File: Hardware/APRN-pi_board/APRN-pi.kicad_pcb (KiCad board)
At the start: 2 copper layers, 65 x 56.5 mm, 31 parts, among them J1 Raspberry_Pi_2_3, J2 Conn_Coaxial, J3 Amplifier Jumper, J4 Screw_Terminal_01x02, J5 AudioJack4, Q1 MMBT3906, U1 DRA818V, U2 L7805

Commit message: Add thanks
@ka2qfx
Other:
- board text added: "Made with help from KA2QFX and others And: #hamradio on libera.chat https://github.com/KenwoodFox/APRN-pi"
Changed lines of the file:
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@@
   (gr_line (start 109 118.5) (end 109 68) (layer "Edge.Cuts") (width 0.1))
   (gr_line (start 171 121.5) (end 112 121.5) (layer "Edge.Cuts") (width 0.1))
+  (gr_text "Made with help from KA2QFX and others\n\nAnd:\n#hamradio on libera.chat\n\nhttps://github.com/KenwoodFox/APRN-pi" (at 139.5 79.5) (layer "B.SilkS")
+    (effects (font (size 1.5 1.5) (thickness 0.3)) (justify mirror))
+  )
   (gr_text "APRN-Pi\nDesign by KW1FOX\n${FULL_REVISION}" (at 154.5 85) (layer "F.SilkS")
     (effects (font (size 1.27 1.27) (thickness 0.15)) (justify left))

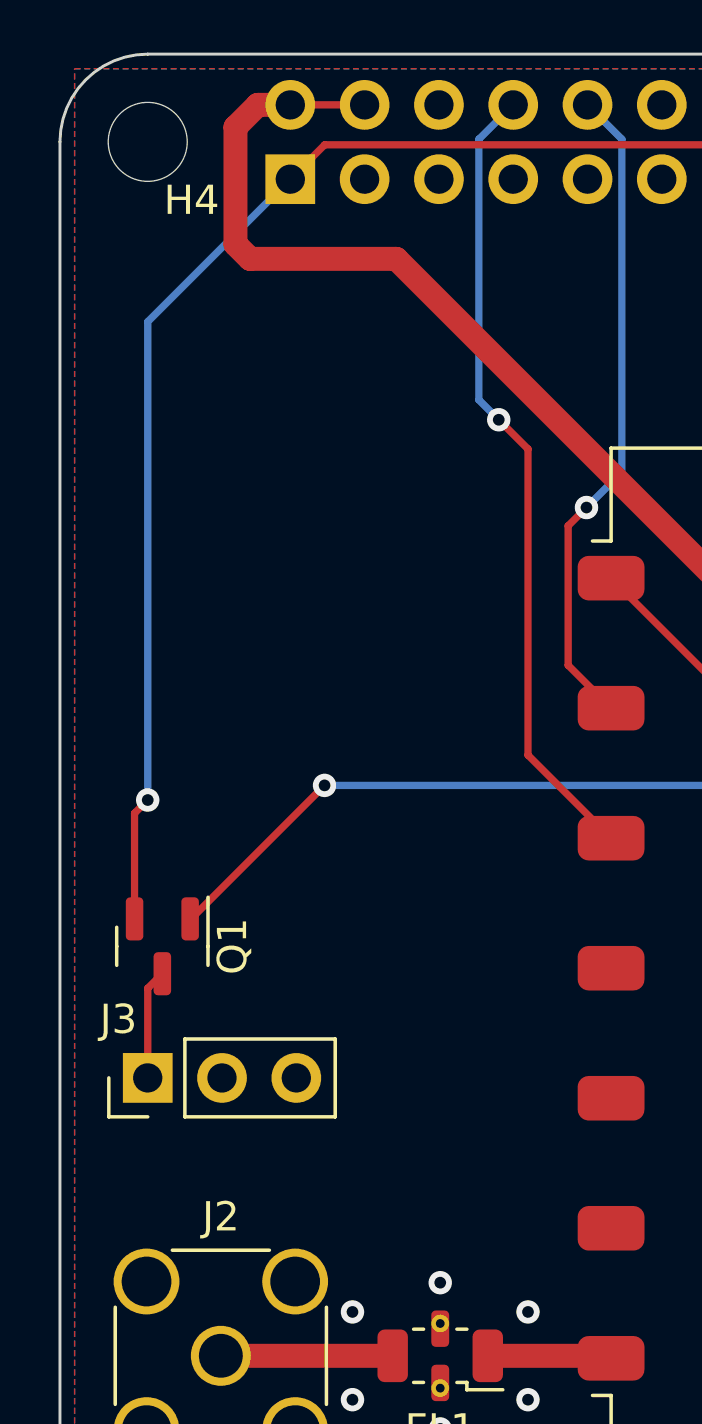
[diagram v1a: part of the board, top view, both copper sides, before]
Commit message: add i2c breakout
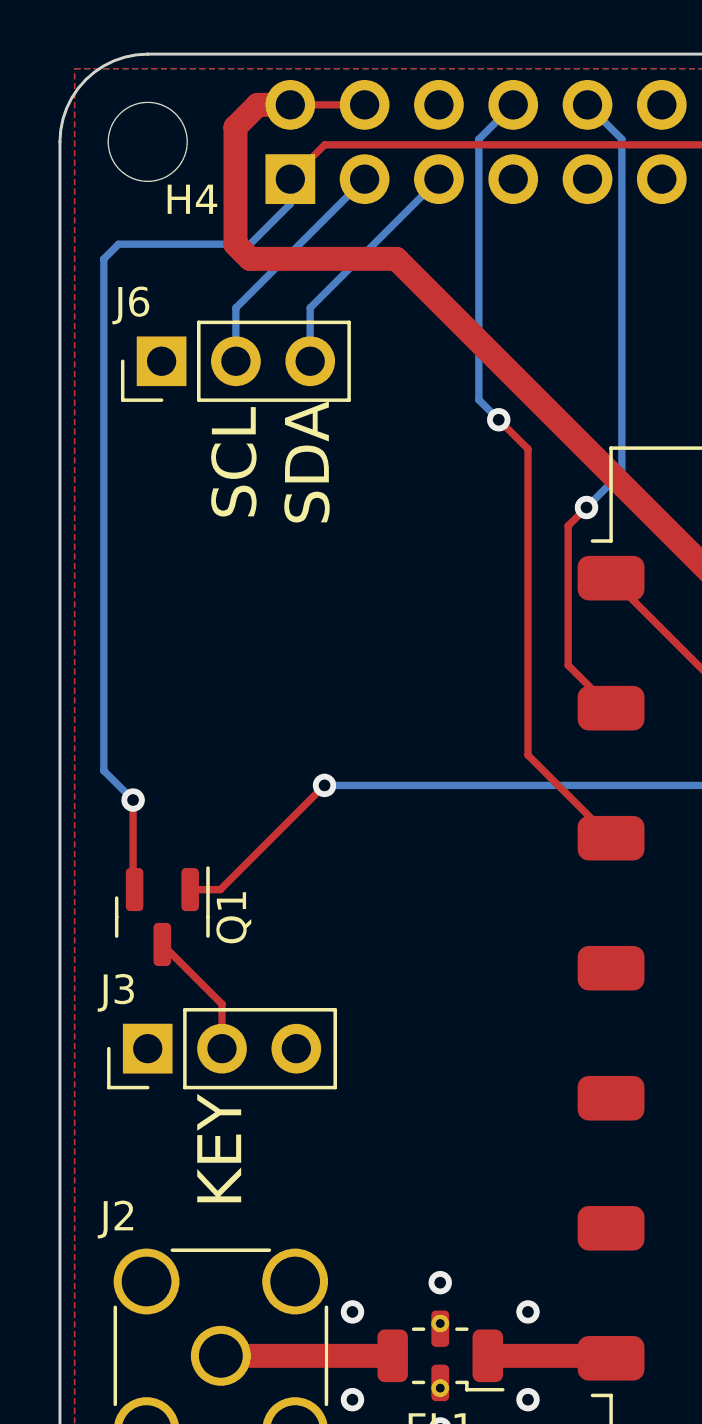
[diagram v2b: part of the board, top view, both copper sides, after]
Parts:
- added J6: i2c Jumper, Connector_PinHeader_2.54mm:PinHeader_1x03_P2.54mm_Vertical, F.Cu at (112.5, 75.5)
- moved J3 1.00 mm to (112.0, 99.0)
- moved Q1 1.00 mm to (112.5, 94.5)
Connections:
- J1 pad 3: unconnected-(J1-Pad3) -> SCL
- J1 pad 5: unconnected-(J1-Pad5) -> SDA
- J3 pad 1: Net-(J3-Pad1) -> GND
- J3 pad 2: GND -> Net-(J3-Pad2)
- J3 pad 3: unconnected-(J3-Pad3) -> GND
- Q1 pad 3: Net-(J3-Pad1) -> Net-(J3-Pad2)
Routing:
- net SCL: track 0.00 -> 8.05 mm
- net SDA: track 0.00 -> 8.05 mm
- net Net-(J3-Pad2): track 0.00 -> 4.41 mm
- net Net-(J3-Pad1): track 3.77 -> 0.00 mm
- net +3V3: track 84.3 -> 86.9 mm
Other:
- board text added: "KEY"
- board text added: "SCL"
- board text added: "SDA"

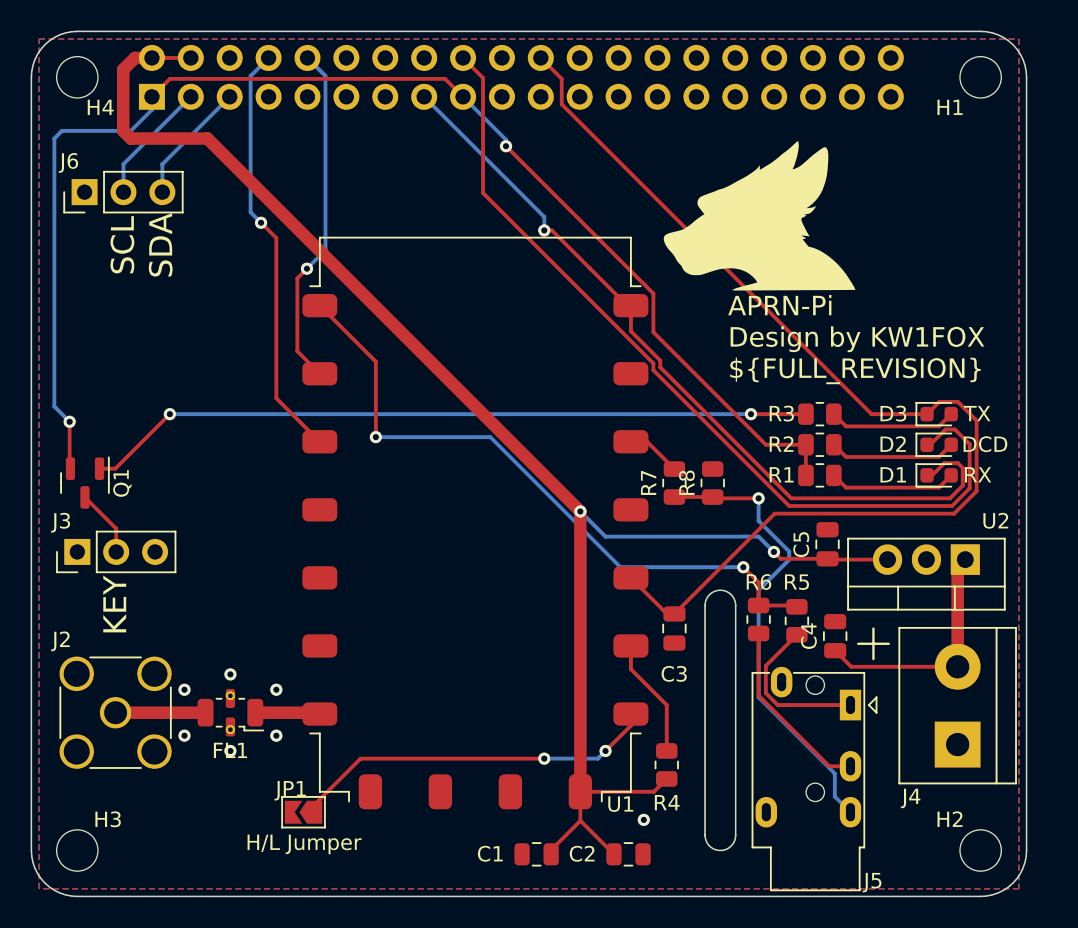
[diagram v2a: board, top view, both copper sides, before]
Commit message: This board will tottally need a rewiring
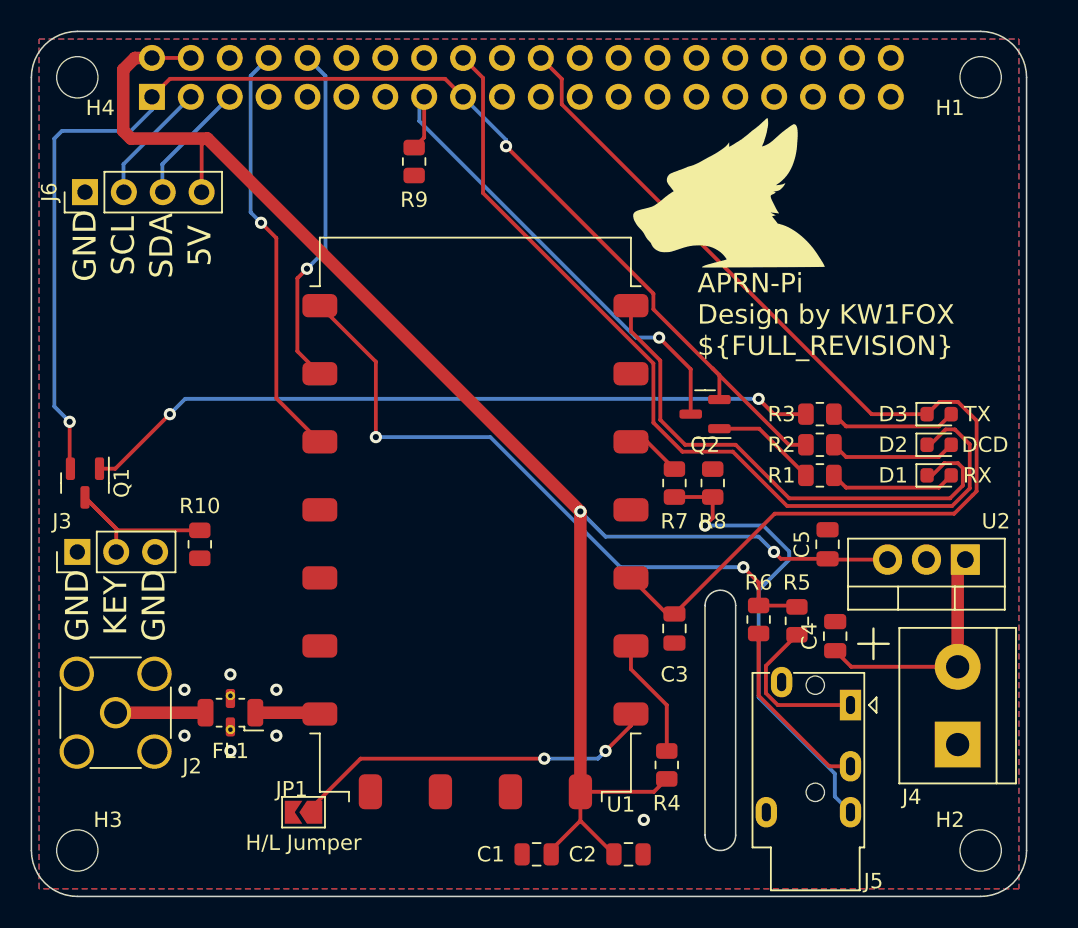
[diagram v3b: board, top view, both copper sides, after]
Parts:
- added Q2: MMBT3906, Package_TO_SOT_SMD:SOT-23, F.Cu at (153.0, 90.0)
- added R10: 10k, Resistor_SMD:R_0805_2012Metric, F.Cu at (120.0, 98.5)
- added R9: 10k, Resistor_SMD:R_0805_2012Metric, F.Cu at (134.0, 73.5)
- J6: value i2c Jumper -> Conn_01x04; footprint Connector_PinHeader_2.54mm:PinHeader_1x03_P2.54mm_Vertical -> Connector_PinHeader_2.54mm:PinHeader_1x04_P2.54mm_Vertical
- moved L1 2.50 mm to (154.5, 75.5)
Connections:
- D1 pad 1: GPIO22 -> SQL
- J6 pad 2: SCL -> SDA
- J6 pad 3: SDA -> SCL
- R1 pad 1: +3V3 -> Net-(R1-Pad1)
- U1 pad 1: GPIO22 -> SQL
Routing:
- net SQL: track 0.00 -> 34.7 mm
- net GPIO22: track 52.1 -> 32.2 mm
- net Net-(Q1-Pad3): track 4.41 -> 12.8 mm
- net Net-(R1-Pad1): track 0.00 -> 6.91 mm
- net +5V: track 102.5 -> 106.2 mm
- net GPIO24: track 56.8 -> 58.8 mm
- net Net-(J5-PadR2): track 30.2 -> 31.1 mm
- net Net-(Q1-Pad1): track 47.6 -> 48.4 mm
- net +3V3: track 86.9 -> 86.2 mm
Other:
- board text added: "5V"
- board text added: "GND"

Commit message: misc
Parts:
- moved L1 1.00 mm to (155.5, 75.5)
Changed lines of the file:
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@@
   )
   (footprint "KenwoodFox:KITSUNE_LOGO" (layer "F.Cu")
-    (at 154.5 75.5)
+    (at 155.5 75.5)
     (property "Sheetfile" "APRN-pi.kicad_sch")
     (property "Sheetname" "")
@@
     (effects (font (size 1.5 1.5) (thickness 0.3)))
   )
-  (gr_text "APRN-Pi\nDesign by KW1FOX\n${FULL_REVISION}" (at 152.5 83.5) (layer "F.SilkS")
+  (gr_text "APRN-Pi\nDesign by KW1FOX\n${FULL_REVISION}" (at 153.5 83.5) (layer "F.SilkS")
     (effects (font (size 1.27 1.27) (thickness 0.15)) (justify left))
   )

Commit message: more logos
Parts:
- added L2: KITSUNE_LOGO, KenwoodFox:KITSUNE_LOGO, B.Cu at (134.5, 92.5)
- added REF**: OSHW-Symbol_8.9x8mm_SilkScreen, Symbol:OSHW-Symbol_8.9x8mm_SilkScreen, B.Cu at (146.5, 92.5)

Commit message: Use upstream
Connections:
- J6 pad 2: SDA -> SCL
- J6 pad 3: SCL -> SDA
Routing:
- net Net-(R4-Pad1): track 7.83 -> 8.49 mm

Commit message: Do some pcb layout
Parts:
- moved C5 2.69 mm to (158.5, 97.5), turned to 180 degrees
- moved R7 1.41 mm to (150.0, 95.5)
- moved R8 1.41 mm to (152.5, 95.5)
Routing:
- net GPIO25: track 71.4 -> 66.6 mm, vias 0 -> 2
- net +5V: track 106.2 -> 109.2 mm, vias 2 -> 0
- net Net-(J5-PadR2): track 31.1 -> 29.9 mm
- net TX_AUDIO: track 42.8 -> 41.9 mm
- net Net-(C4-Pad1): track 15.6 -> 16.3 mm
- net GND: vias 7 -> 9

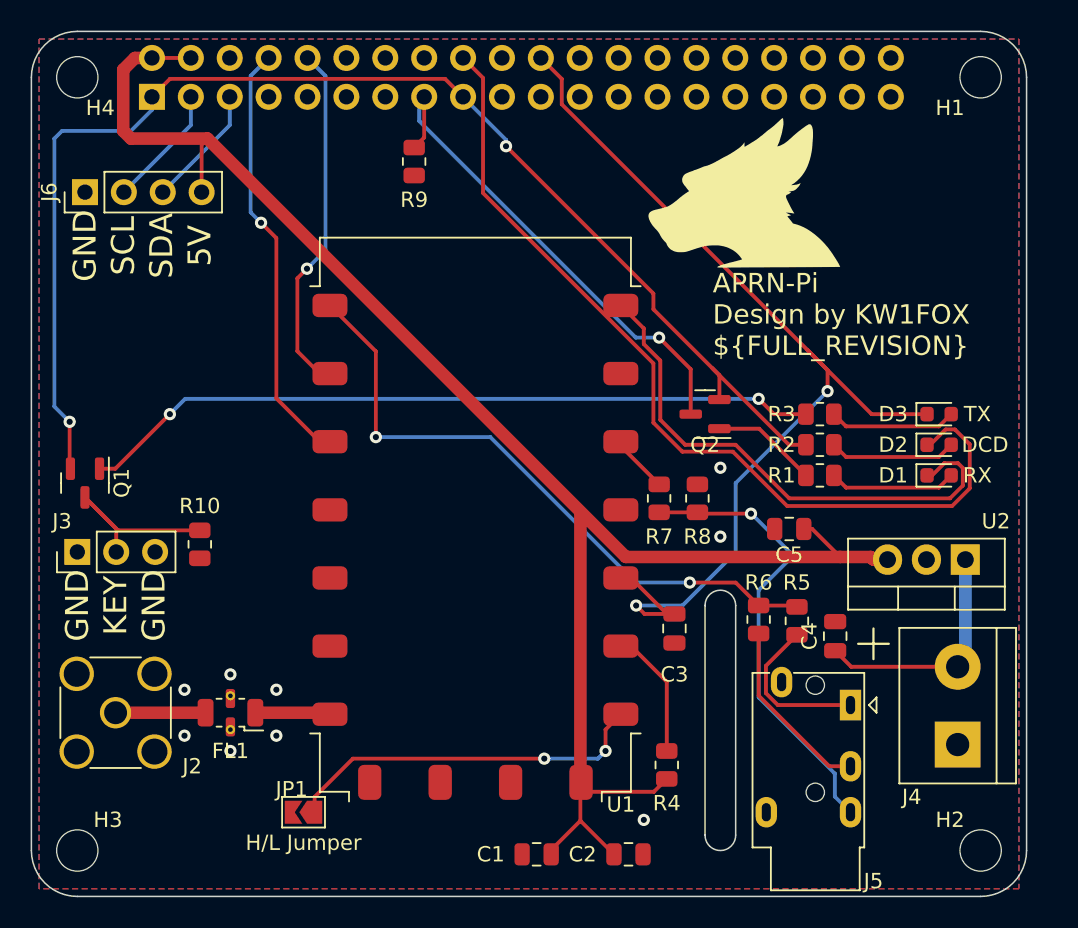
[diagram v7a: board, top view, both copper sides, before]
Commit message: Refactor wiring
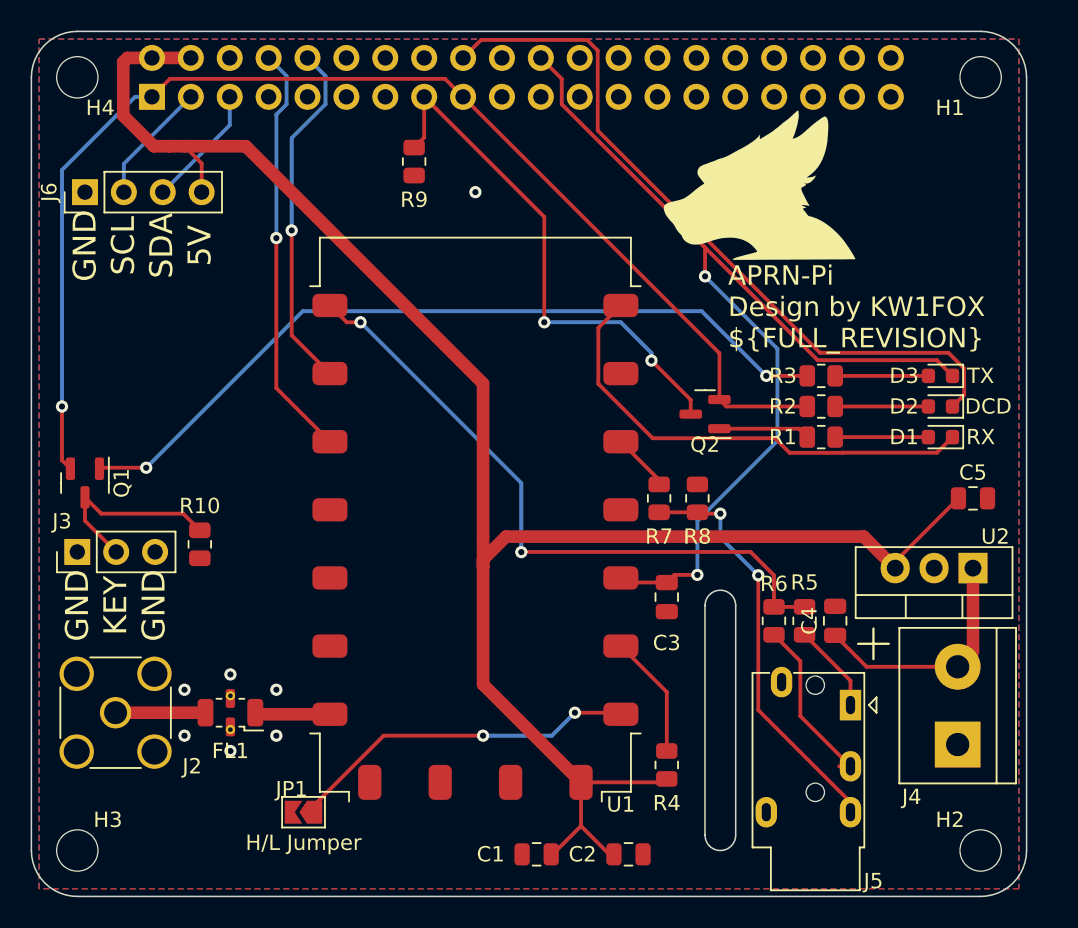
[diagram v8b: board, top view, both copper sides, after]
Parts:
- moved C5 12.2 mm to (170.5, 95.5), turned to 0 degrees
- moved D1 2.50 mm to (168.4, 91.5), turned to 180 degrees
- moved D2 2.50 mm to (168.4, 89.5), turned to 180 degrees
- moved D3 2.50 mm to (168.4, 87.5), turned to 180 degrees
- moved R1 2.50 mm to (160.6, 91.5)
- moved R2 2.50 mm to (160.6, 89.5)
- moved R3 2.50 mm to (160.6, 87.5)
- moved C3 2.11 mm to (150.5, 102.0)
- moved L1 1.12 mm to (156.5, 75.0)
- moved R6 1.00 mm to (157.5, 103.5)
- moved C4 1.00 mm to (161.5, 103.5)
- moved U2 0.75 mm to (170.5, 100.1)
- moved R5 0.50 mm to (159.5, 103.5)
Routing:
- net +5V: track 109.2 -> 120.6 mm
- net GPIO24: track 58.8 -> 48.0 mm
- net +3V3: track 86.2 -> 81.5 mm, vias 2 -> 1
- net Net-(J5-PadT): track 10.5 -> 5.83 mm
- net SQL: track 35.0 -> 31.1 mm
- net Net-(Q1-Pad1): track 48.4 -> 52.2 mm
- net Net-(J5-PadR2): track 29.9 -> 27.1 mm, vias 1 -> 2
- net Net-(D3-Pad2): track 8.32 -> 6.09 mm
- net Net-(D2-Pad2): track 8.32 -> 6.09 mm
- net Net-(D1-Pad2): track 8.32 -> 6.09 mm
- net GPIO22: track 32.2 -> 34.4 mm, vias 1 -> 2
- net TX_AUDIO: track 41.9 -> 43.0 mm
- net H/L: track 24.1 -> 23.0 mm
- net Net-(Q2-Pad1): track 6.91 -> 5.97 mm
- net GPIO25: track 66.6 -> 67.4 mm
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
